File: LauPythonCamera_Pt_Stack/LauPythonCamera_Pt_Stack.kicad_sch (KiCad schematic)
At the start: 46 parts, among them J1 DF40C-80DP (Bank A), J2 DF40C-80DP (Bank B), J3 DF40C-50DP (Control), U1 NOIP1SN1300A-QDI, U2 AP2112K-1.8 LDO, U3 LoadSw Rdson<=100m, U4 ADP7158-3.3

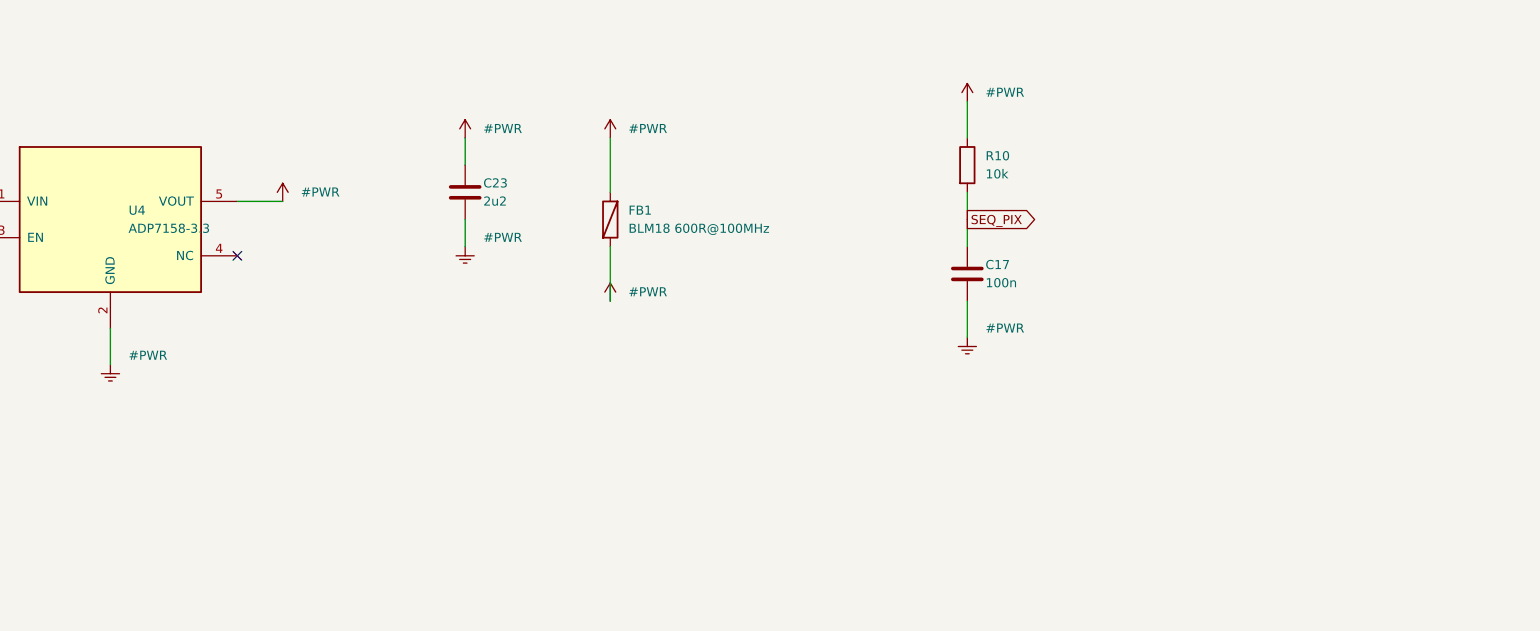
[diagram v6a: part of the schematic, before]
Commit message: fix(camera): D1 (anti-sequenced power-down) + D3 (U4 was the wrong part)
The last two defects from the schematic audit. Both were mine.

===========================================================================
D1 — POWER-DOWN WAS ANTI-SEQUENCED, not merely unsequenced
===========================================================================

Root cause I had missed: VDD_SYS OUTLIVES +3V3_SYS. The Pt's 3.3 V regulator is
fed FROM VDD, so on power-down the 3.3 V rail dies while VDD is still coasting.
And vdd_pix was the ONLY rail I fed from VDD_SYS.

So on every power-down, vdd_33 and vdd_18 collapsed while vdd_pix sat at 3.3 V
into a dead core for ~9 ms (14 uF of bulk against a 5 mA load), forward-biasing
internal junctions against a 100 mA latch-up rating. Datasheet p.18: "first
vdd_pix, second vdd_33, and finally vdd_18. Any other sequence can cause high
peak currents."

The board delivered exactly the reverse, on every one of the three edges. On
every unplug and every reset. My README called this "possibly nothing".

FIX (3 parts):
  Q1  PMOS. source=+3V3_PIX, gate=+3V3_SYS, drain -> R16 (47R) -> GND
        normal     Vgs = 3.3-3.3 = 0     -> OFF
        startup    Vgs = 3.3-0   = +3.3  -> OFF (it is a PMOS)
        power-down +3V3_SYS drops below vdd_pix by |Vth| -> ON, dumps the rail
      => vdd_pix can never sit more than ~|Vth| above vdd_33.
      => when vdd_33 = 0, vdd_pix <= ~0.9 V. The failure mode is gone.

  D1  diode across R10. NOT OPTIONAL. Without it, SEQ_PIX decays with a 1 ms RC
      after +3V3_CAM dies, so U4 keeps regulating 3.3 V into a conducting Q1 --
      the clamp fights the regulator. The diode collapses U4's enable the instant
      +3V3_CAM falls, and is reverse-biased on the way up so the slow ramp is
      preserved.
      Deliberately NOT fitted across R8: vdd_18 must be the LAST rail down.

===========================================================================
D3 — U4 WAS THE WRONG PART, AND MY ACCURACY SPEC WAS ALSO WRO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
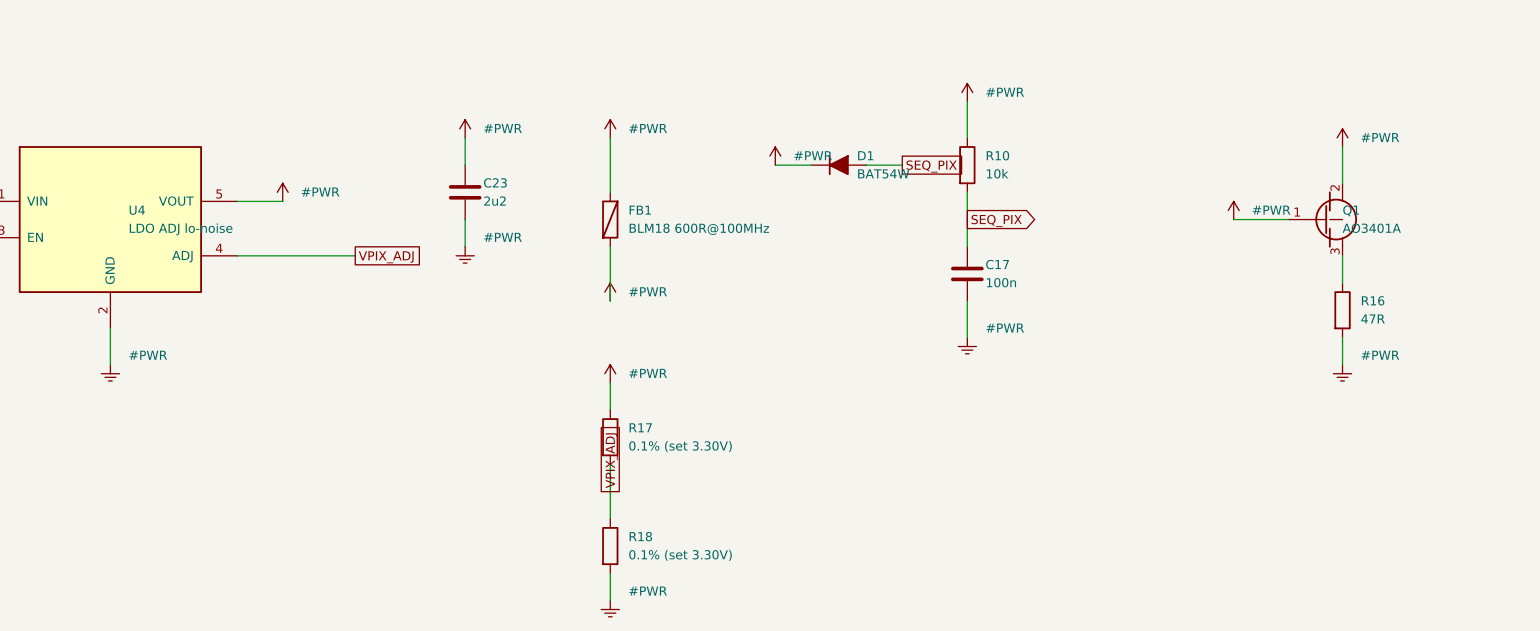
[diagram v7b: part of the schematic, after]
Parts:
- removed U4: ADP7158-3.3, Package_TO_SOT_SMD:SOT-23-5, symbol LauSensors:REG_5PIN_EN
- added D1: BAT54W, Diode_SMD:D_SOD-323, symbol Device:D
- added Q1: AO3401A, Package_TO_SOT_SMD:SOT-23, symbol Device:Q_PMOS_GSD
- added R16: 47R, Resistor_SMD:R_0402_1005Metric, symbol Device:R
- added R17, R18: 0.1% (set 3.30V), Resistor_SMD:R_0402_1005Metric, symbol Device:R
- added U4: LDO ADJ lo-noise, Package_TO_SOT_SMD:SOT-23-5, symbol LauSensors:REG_ADJ_EN
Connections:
- net +3V3_CAM: now also D1.1 (K)
- net +3V3_PIX: now also Q1.2 (S)
- net +3V3_PIX_RAW: now also R17.1, U4.5 (VOUT)
- net +3V3_SYS: now also Q1.1 (G)
- net GND: now also R16.2, R18.2, U4.2 (GND)
- net SEQ_PIX: now also D1.2 (A), U4.3 (EN)
- net VDD_SYS: now also U4.1 (VIN)
- new net: Q1.3 (D), R16.1
- new net VPIX_ADJ: R17.2, R18.1, U4.4 (ADJ)
- no-connect marks 102 -> 101

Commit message: fix(camera): REBUILD the power tree — it was architecturally wrong
The power/analog audit found the power section was not buggy, it was BACKWARDS.
VDD is confirmed 5 V (USB-C), which makes the correct architecture available.

WHAT WAS WRONG
--------------
* vdd_33 -- the sensor's ANALOG 3.3 V domain, 140 mA -- came through a bare LOAD
  SWITCH off the Pt's +3V3_SYS, which is a 4 A ADP5052 buck feeding an XC7A100T
  and DDR3L. A load switch has NO PSRR. Every FPGA and DDR3 transient went
  straight into the sensor's analog supply.
  Meanwhile the 5 mA vdd_pix got the ultra-low-noise LDO. Backwards.

* The DC budget did not close. At +/-2% on the Pt's rail there was 34 mV of total
  IR budget for connector + trace + switch. At +/-3%, NO Rds(on) works -- out of
  spec at zero ohms.

* ADP7158's abs-max Vin is 7 V. VDD_SYS had been specified 5-12 V. At 12 V the
  part is DESTROYED, and a shorted pass element puts 12 V onto vdd_pix -> dead
  sensor. My README defended this with "even at 12 V the dissipation is <90 mW --
  no thermal issue". The part dies on VOLTAGE, not heat. I answered a question
  nobody asked.

* ADP7158 is a 2 A part in 10-lead LFCSP / 8-lead SOIC -- never a SOT-23-5. The
  generic 5-pin symbol mapped VDD_SYS onto VOUT and GND onto VOUT_SENSE.

* And "+/-1% or better", which I wrote as the accuracy requirement, is NOT enough:
  the vdd_pix window is +/-1.52%, and a part sold as "+/-1%" is typically +/-1% at
  25 C and +/-2% OVER TEMPERATURE -> 3.234-3.366 V, outside at BOTH ends.

THE NEW TREE
------------
    VDD_SYS 5V --+--> U2  LDO 1.8 V           -------------> +1V8_CAM  vdd_18   80 mA
                 +--> U3  LDO 3.3 V LOW-NOISE --+----------> +3V3_CAM  vdd_33  140 mA
                                                +-- FB1 ---> +3V3_PIX  vdd_pix   5 mA

* vdd_33 now comes from a REAL low-noise LDO. PSRR and tolerance both fixed at
  once -- the two biggest defects, gone with one part change.

* vdd_pix IS vdd_33, through the bead. Both are 3.3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
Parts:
- removed D1: BAT54W, Diode_SMD:D_SOD-323, symbol Device:D
- removed Q1: AO3401A, Package_TO_SOT_SMD:SOT-23, symbol Device:Q_PMOS_GSD
- removed R15: 10k, Resistor_SMD:R_0402_1005Metric, symbol Device:R
- removed R16: 47R, Resistor_SMD:R_0402_1005Metric, symbol Device:R
- removed R17, R18: 0.1% (set 3.30V), Resistor_SMD:R_0402_1005Metric, symbol Device:R
- removed U4: LDO ADJ lo-noise, Package_TO_SOT_SMD:SOT-23-5, symbol LauSensors:REG_ADJ_EN
- added C24, C25, C32: 10u, Capacitor_SMD:C_0805_2012Metric, symbol Device:C
- added C26, C27, C28, C29, C30, C33: 100n, Capacitor_SMD:C_0402_1005Metric, symbol Device:C
- added C31: 10u (U3 Cout), Capacitor_SMD:C_0805_2012Metric, symbol Device:C
- C12, C13, C14, C18, C19: value 10u -> 10n; footprint Capacitor_SMD:C_0805_2012Metric -> Capacitor_SMD:C_0402_1005Metric
- C15, C16, C17, C20, C21, C22: value 100n -> 10n
- C23: value 2u2 -> 10u; footprint Capacitor_SMD:C_0402_1005Metric -> Capacitor_SMD:C_0805_2012Metric
- R10: value 10k -> 1k
- R12: value 1k -> 10k
- U2: value AP2112K-1.8 LDO -> AP2112K-1.8
- U3: value LoadSw Rdson<=100m -> LDO 3V3 lo-noise
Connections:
- net +3V3_PIX_RAW is gone; now on net +3V3_CAM: C23.1, FB1.1
- net +1V8_CAM: now also C16.1, C17.1, C18.1, C24.1, C27.1; no longer C13.1, C21.1
- net +3V3_CAM: now also C13.1, C14.1, C15.1, C26.1, C31.1; no longer C20.1, R10.1
- net +3V3_PIX: now also C19.1, C20.1, C21.1, C25.1, C28.1; no longer C14.1
- net +3V3_SYS: now also R10.1; no longer C18.1, R12.1, R8.1, U2.1 (VIN), U3.1 (VIN)
- net CAM_CLK_PLL: now also R14.1
- net CAM_MOSI: now also R12.1; no longer R13.1
- net CAM_SCK: now also R13.1; no longer R14.1
- net GND: now also R12.2, C24.2, C25.2, C26.2, C27.2, C28.2, C29.2, C30.2, C31.2, C32.2, C33.2
- net SEQ_1V8: now also C29.1; no longer C15.1
- net SEQ_3V3: now also C30.1; no longer C16.1
- net VBSEL_A: now also R10.2; no longer R11.2
- net VBSEL_B: now also R11.2; no longer R12.2
- net VDD_SYS: now also R8.1, U2.1 (VIN), U3.1 (VIN), C32.1, C33.1; no longer C19.1
- removed net SEQ_PIX: C17.1, R10.2
